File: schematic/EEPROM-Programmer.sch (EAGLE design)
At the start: 8 parts

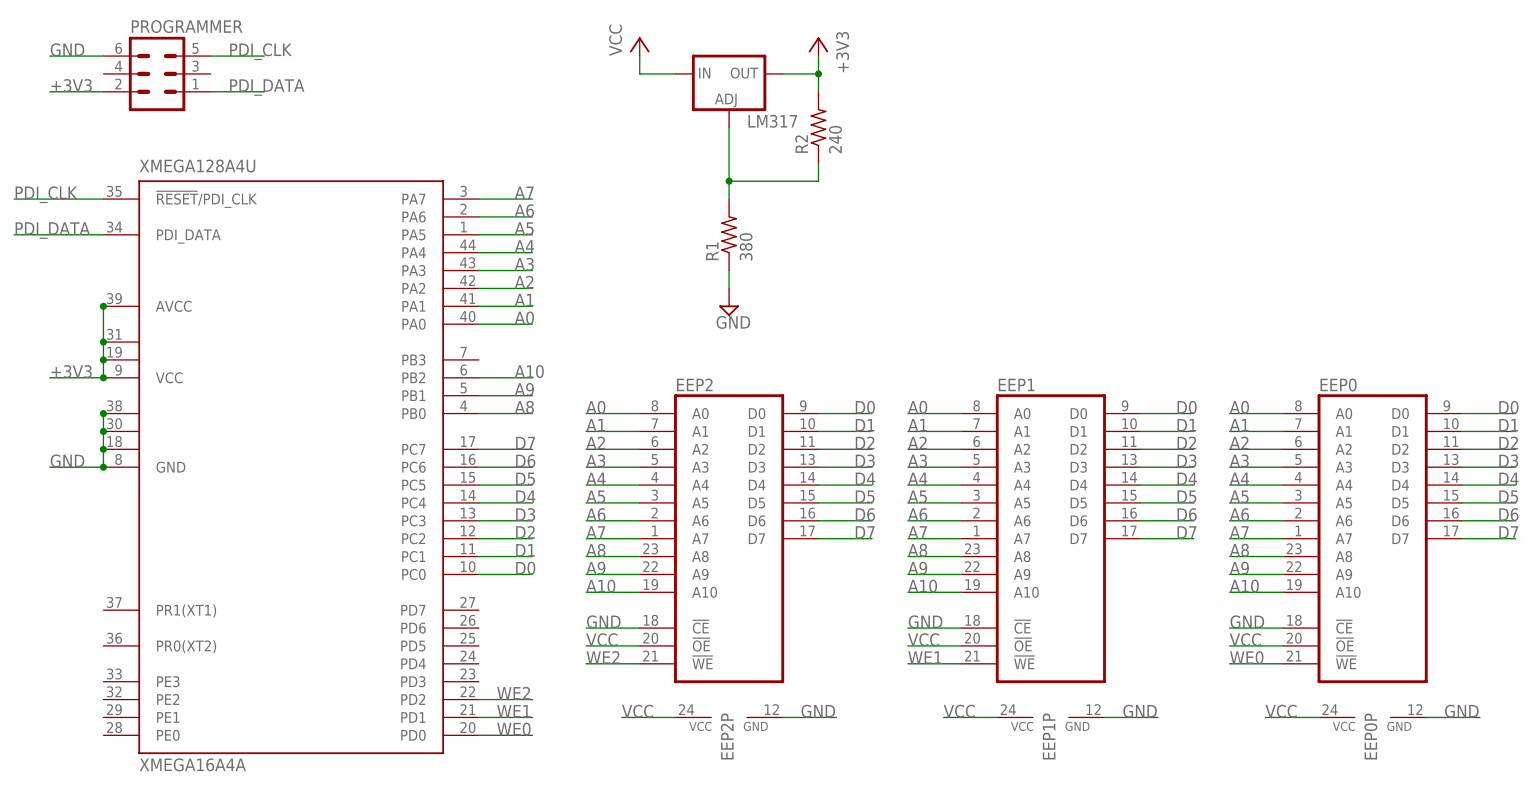
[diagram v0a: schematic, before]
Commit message: Changed the circuit to only write to one EEPROM
Removed all extra control lines and chips.
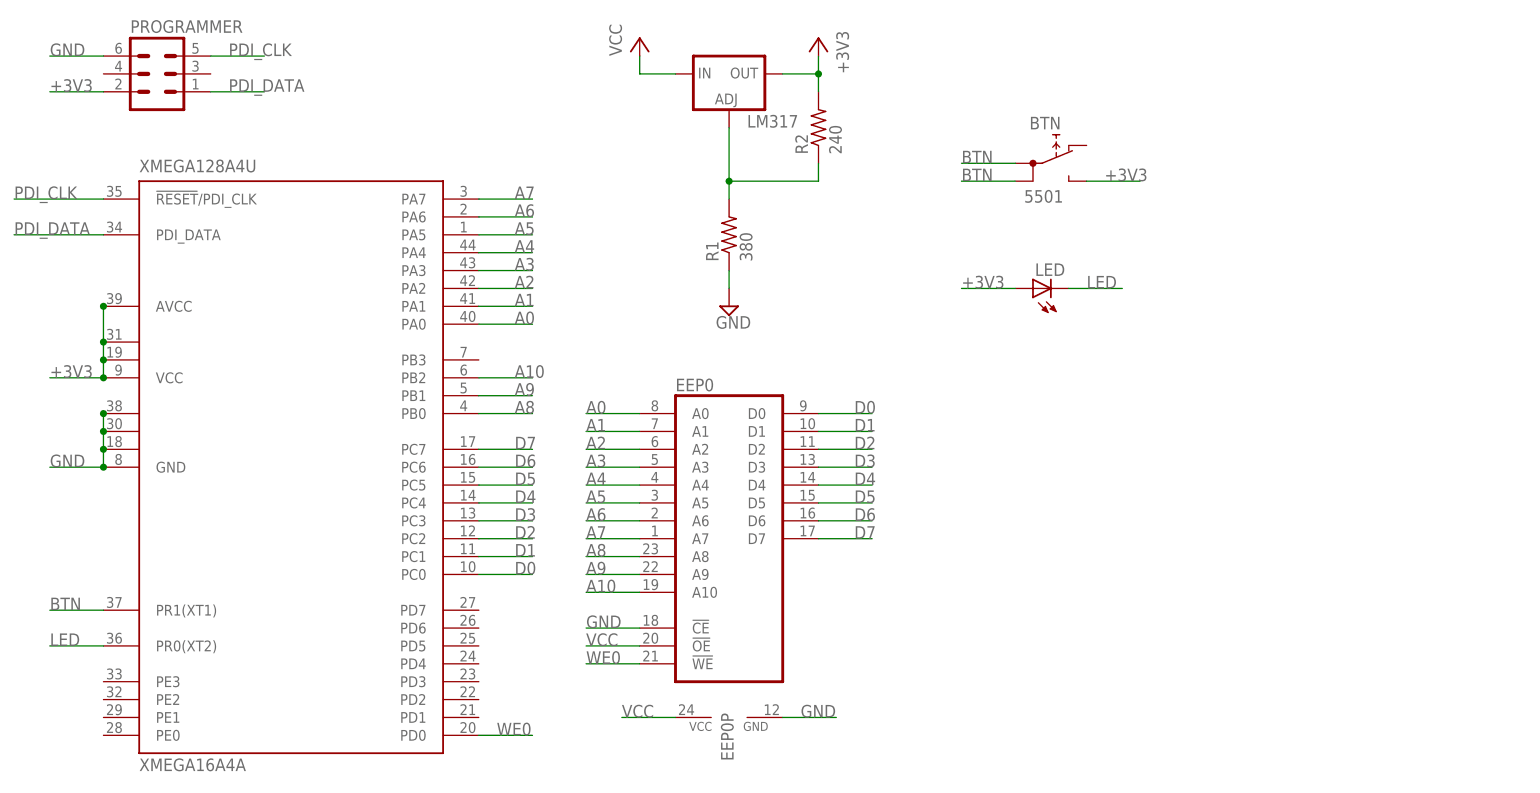
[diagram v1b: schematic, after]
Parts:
- removed EEP1, EEP2: (no value), memory:2816
- added BTN: 5501, switch:5501
- added LED: (no value), led:LED3MM
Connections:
- removed net WE1: EEP1A.!WE, XMEGA128A4U.PD1
- removed net WE2: EEP2A.!WE, XMEGA128A4U.PD2
- new net BTN: BTN.1A, BTN.1B, XMEGA128A4U.PR1(XT1)
- new net LED: LED.C, XMEGA128A4U.PR0(XT2)
- net +3V3: now also BTN.NO, LED.A
- net A0: no longer EEP1A.A0, EEP2A.A0
- net A1: no longer EEP1A.A1, EEP2A.A1
- net A10: no longer EEP1A.A10, EEP2A.A10
- net A2: no longer EEP1A.A2, EEP2A.A2
- net A3: no longer EEP1A.A3, EEP2A.A3
- net A4: no longer EEP1A.A4, EEP2A.A4
- net A5: no longer EEP1A.A5, EEP2A.A5
- net A6: no longer EEP1A.A6, EEP2A.A6
- net A7: no longer EEP1A.A7, EEP2A.A7
- net A8: no longer EEP1A.A8, EEP2A.A8
- net A9: no longer EEP1A.A9, EEP2A.A9
- net D0: no longer EEP1A.D0, EEP2A.D0
- net D1: no longer EEP1A.D1, EEP2A.D1
- net D2: no longer EEP1A.D2, EEP2A.D2
- net D3: no longer EEP1A.D3, EEP2A.D3
- net D4: no longer EEP1A.D4, EEP2A.D4
- net D5: no longer EEP1A.D5, EEP2A.D5
- net D6: no longer EEP1A.D6, EEP2A.D6
- net D7: no longer EEP1A.D7, EEP2A.D7
- net GND: no longer EEP1A.!CE, EEP1P.GND, EEP2A.!CE, EEP2P.GND
- net VCC: no longer EEP1A.!OE, EEP1P.VCC, EEP2A.!OE, EEP2P.VCC
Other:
- moved on the sheet: EEP0, EEP0P

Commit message: Used Freerouting to route the board
Renamed a few lines.
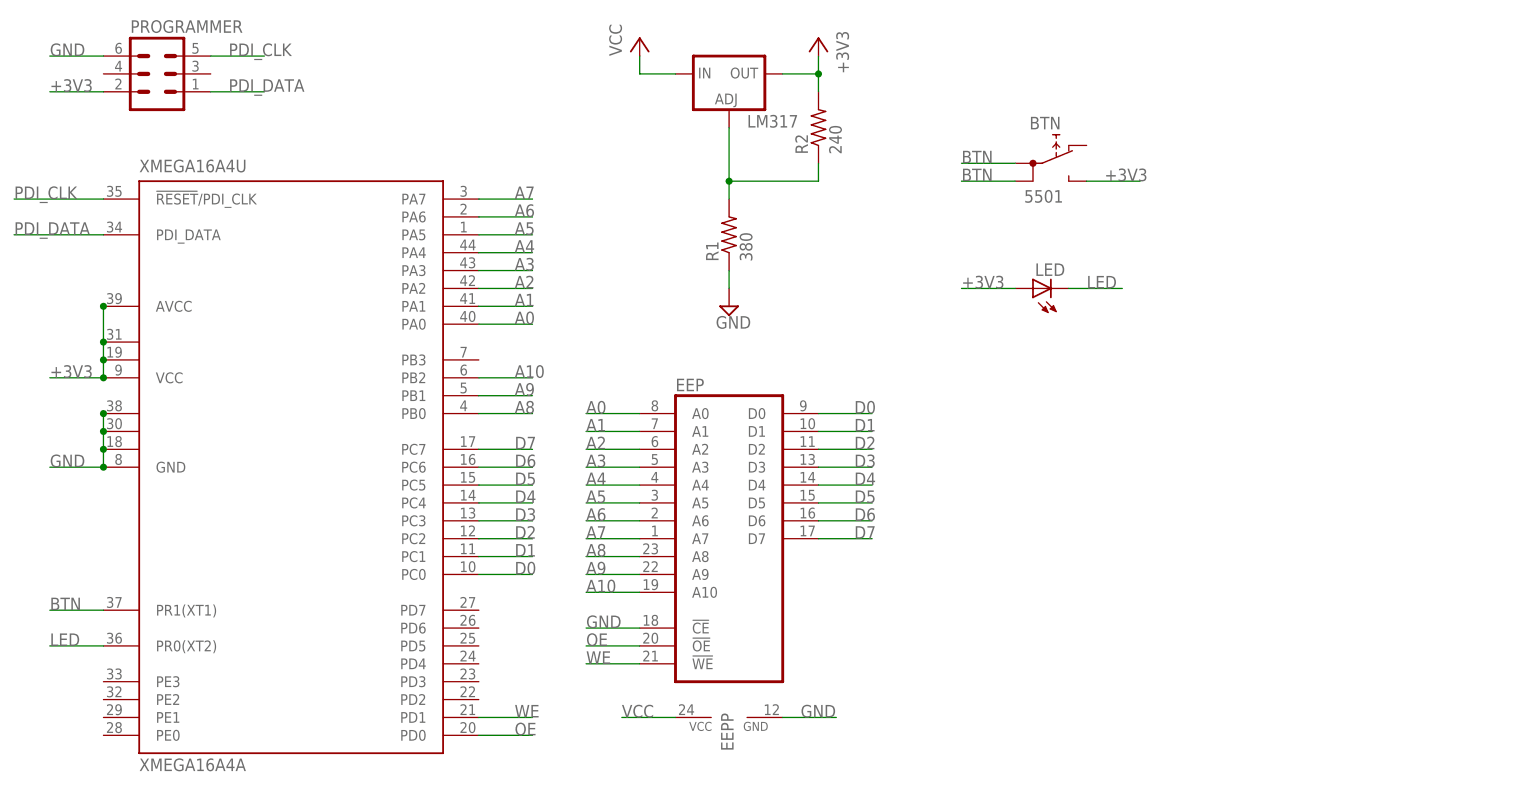
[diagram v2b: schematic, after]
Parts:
- renumbered EEP0 to EEP, XMEGA128A4U to XMEGA16A4U
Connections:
- removed net WE0: EEPA.!WE, XMEGA16A4U.PD0
- new net OE: EEPA.!OE
- new net WE: EEPA.!WE
- net VCC: no longer EEPA.!OE
